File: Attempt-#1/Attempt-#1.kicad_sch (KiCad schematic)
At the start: 1 part

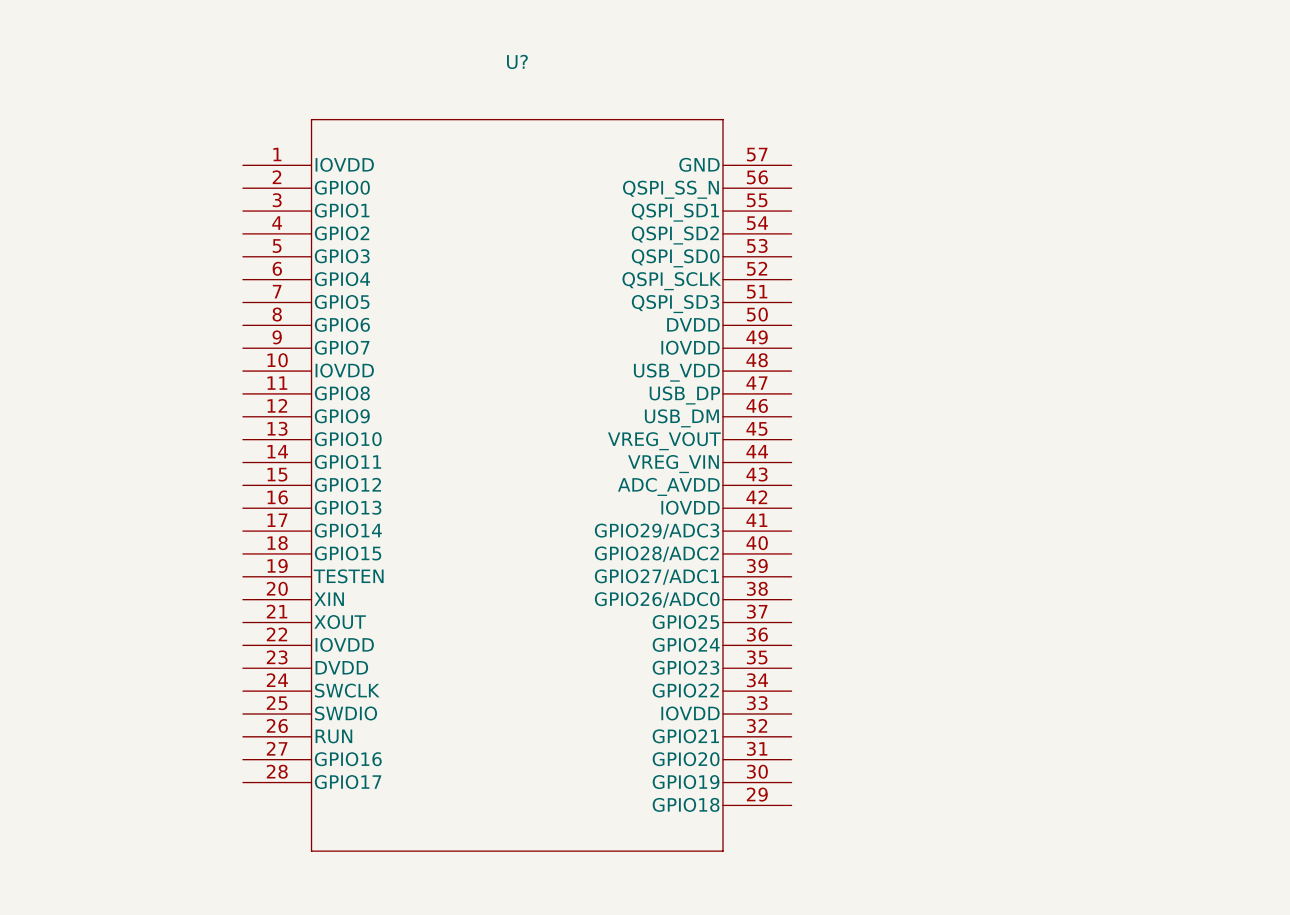
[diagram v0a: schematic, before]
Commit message: Started basic pinout for neccescary parts of RP2040
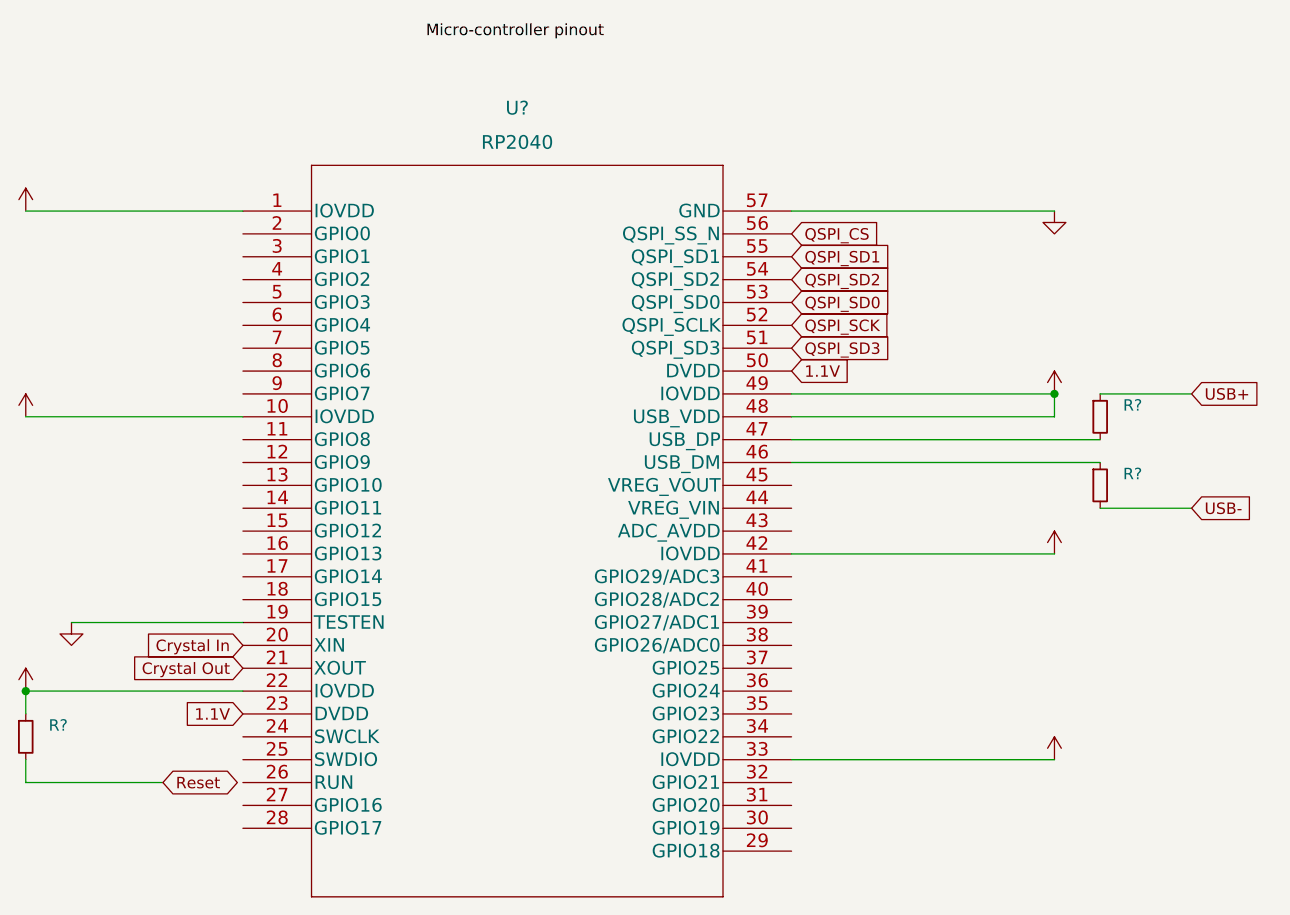
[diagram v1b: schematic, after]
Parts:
- added R? (x3): (no value), symbol Device:R_Small
- U?: value (none) -> RP2040; footprint (none) -> IC57_RP2040
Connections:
- net +3V3: now reaches U?.1 (IOVDD)
- net +3V3: now also U?.10 (IOVDD), U?.22 (IOVDD), U?.33 (IOVDD), U?.42 (IOVDD), U?.48 (USB_VDD), U?.49 (IOVDD), R?.1
- net GND: now reaches U?.19 (TESTEN)
- net GND: now also U?.57 (GND)
- net Crystal In: now reaches U?.20 (XIN)
- net Crystal Out: now reaches U?.21 (XOUT)
- net 1.1V: now reaches U?.23 (DVDD)
- net 1.1V: now also U?.50 (DVDD)
- net at U?.46 (USB_DM): now also R?.1
- net at U?.47 (USB_DP): now also R?.2
- net QSPI_SD3: now reaches U?.51 (QSPI_SD3)
- net QSPI_SCK: now reaches U?.52 (QSPI_SCLK)
- net QSPI_SD0: now reaches U?.53 (QSPI_SD0)
- net QSPI_SD2: now reaches U?.54 (QSPI_SD2)
- net QSPI_SD1: now reaches U?.55 (QSPI_SD1)
- net QSPI_CS: now reaches U?.56 (QSPI_SS_N)
- new net Reset: R?.2
- new net USB+: R?.1
- new net USB-: R?.2
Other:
- moved on the sheet: U?
